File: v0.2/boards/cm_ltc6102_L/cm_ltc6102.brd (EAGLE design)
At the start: 81 x 60 mm, 98 parts, among them J1 10118194-0001LF, U1 ADA4528-2ARMZ-R7, U10 TS5A3159ADBVRDBV6-M, U2 LTC6102IMS8PBF, U3 ADM7170ACPZ-1.3-R7CP_8_21-M, U4 MIC2250-1YD5TSOT-23-5_D5-M, U6 TS3A4751PWRPW14-M, U7 TS5A4624DCKRDCK6-M, X1 PN87520-S

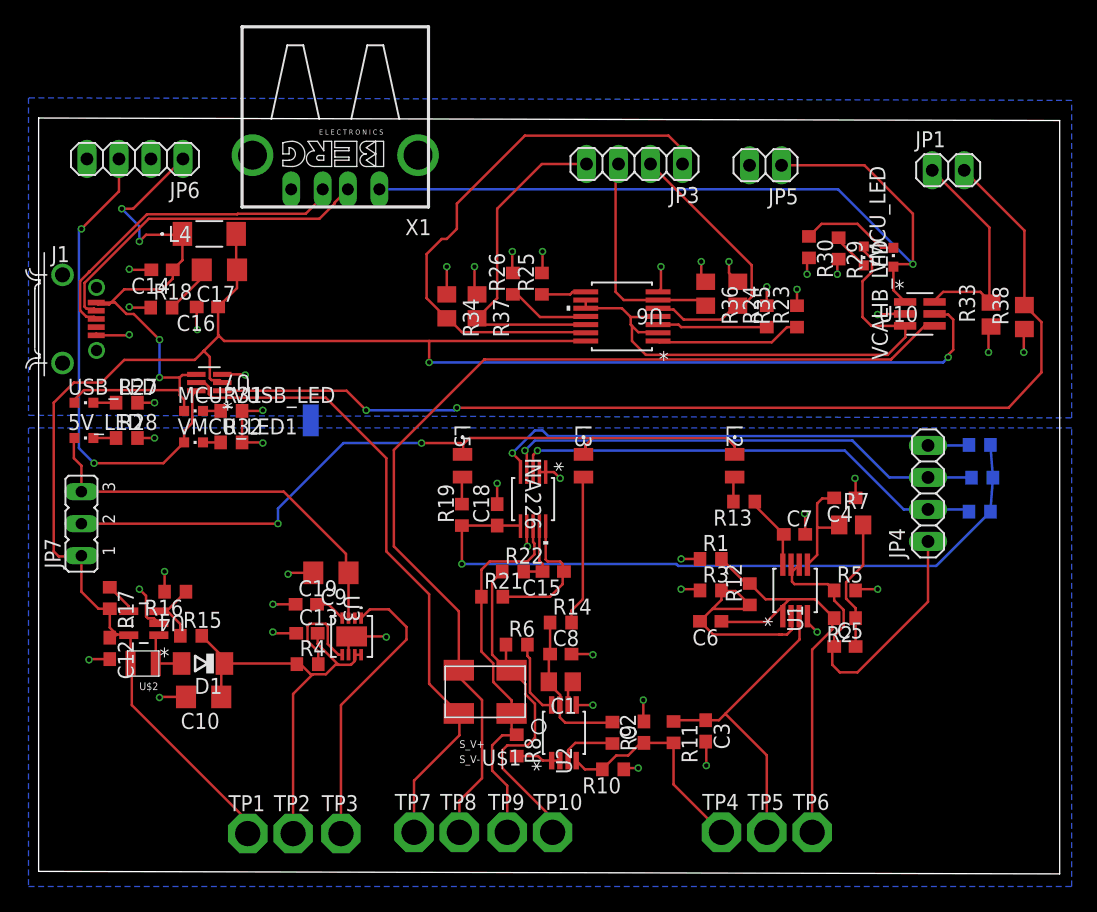
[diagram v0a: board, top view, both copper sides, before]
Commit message: cm_ltc6102_L: modify layout, finish silkscreen
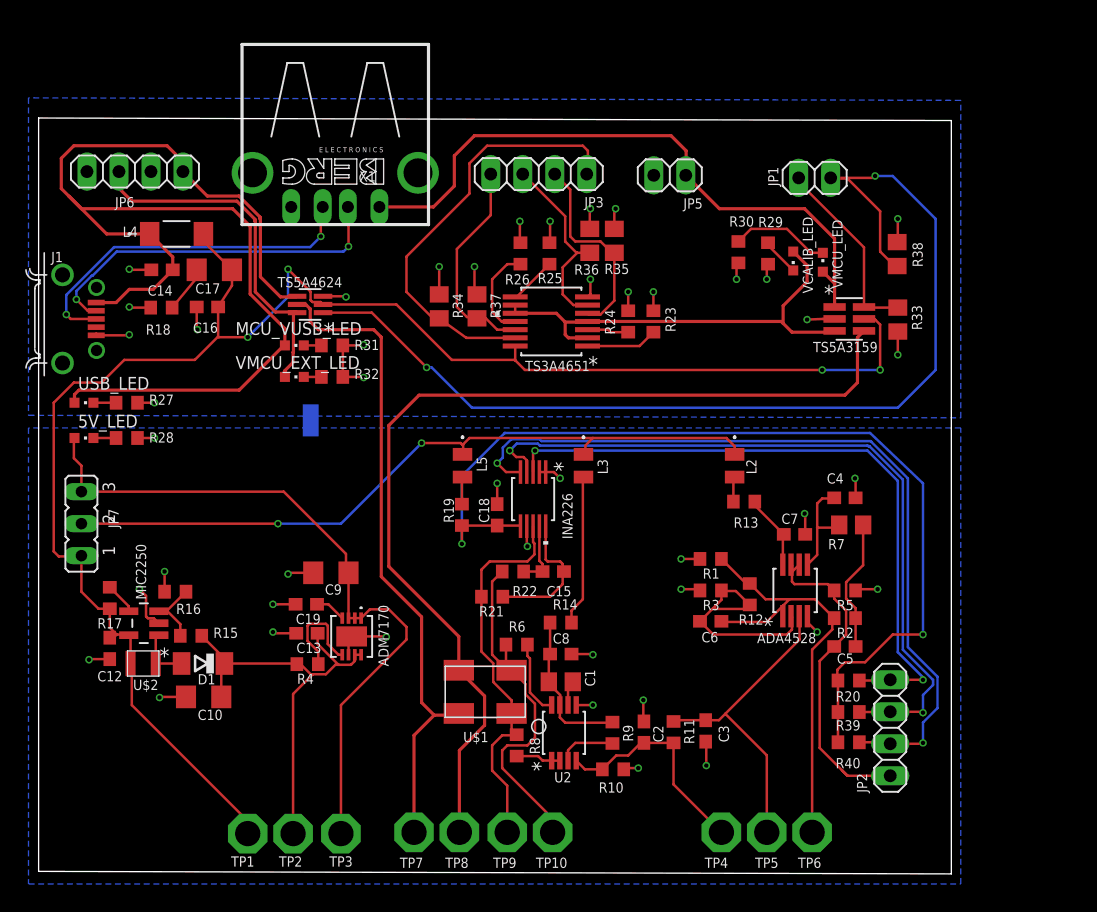
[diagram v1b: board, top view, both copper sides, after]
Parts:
- removed JP4: (no value), pinhead:1X04
- removed U10: TS5A3159ADBVRDBV6-M, texas_instruments:DBV6-M
- removed U6: TS3A4751PWRPW14-M, texas_instruments:PW14-M
- removed U7: TS5A4624DCKRDCK6-M, texas_instruments:DCK6-M
- removed VMCU_LED1: (no value), led:CHIPLED_0603
- added JP2: (no value), pinhead:1X04
- added TS3A4651: TS3A4751PWRPW14-M, texas_instruments:PW14-M
- added TS5A3159: TS5A3159ADBVRDBV6-M, texas_instruments:DBV6-M
- added TS5A4624: TS5A4624DCKRDCK6-M, texas_instruments:DCK6-M
- added VMCU_EXT_LED: (no value), led:CHIPLED_0603
- moved R40 25.8 mm to (64.3, 10.2), flipped to the top
- moved R39 21.4 mm to (64.3, 12.7), flipped to the top
- moved R20 17.0 mm to (64.3, 15.2), flipped to the top
- moved R23 11.4 mm to (48.8, 43.6)
- moved R38 11.3 mm to (68.2, 49.0), turned to 270 degrees
- moved R24 11.0 mm to (46.8, 43.6)
- moved R35 10.7 mm to (45.7, 50.0)
- moved JP1 10.6 mm to (61.6, 55.0)
- moved R36 10.1 mm to (43.8, 50.0)
- moved MCU_VUSB_LED 9.54 mm to (20.3, 41.8)
- moved R31 9.54 mm to (23.3, 41.8)
- moved R32 9.54 mm to (23.3, 39.2)
- moved JP5 7.64 mm to (50.1, 55.2)
- moved JP3 7.64 mm to (39.7, 55.4)
- moved R33 7.41 mm to (68.2, 43.8)
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- renumbered U1 to ADA4528, U3 to ADM7170, U4 to MIC2250
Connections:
- net 5V_F: now also TS3A4651.14, TS5A3159.5, TS5A4624.2; no longer U10.5, U6.14, U7.2
- net 5V_USB: now also TS5A4624.4; no longer U7.4
- net ADC_CM_LOW: now also JP2.1; no longer JP4.1
- net ALERT: now also JP2.4; no longer JP4.2
- net DGND: now also TS3A4651.7, TS5A3159.2, TS5A4624.3; no longer U10.2, U6.7, U7.3
- net N$26: now also VMCU_EXT_LED.C; no longer VMCU_LED1.C
- net N$30: now also TS3A4651.1; no longer U6.1
- net N$31: now also TS3A4651.3; no longer U6.3
- net N$32: now also TS3A4651.8; no longer U6.8
- net N$33: now also TS3A4651.11; no longer U6.11
- net SCL: now also JP2.2; no longer JP4.4
- net SDA: now also JP2.3; no longer JP4.3
- net SW_CTRL_0: now also TS5A3159.6; no longer U10.6
- net SW_CTRL_1: now also TS3A4651.13; no longer U6.13
- net SW_CTRL_2: now also TS3A4651.5; no longer U6.5
- net SW_CTRL_3: now also TS3A4651.6; no longer U6.6
- net SW_CTRL_4: now also TS3A4651.12; no longer U6.12
- net SW_CTRL_PWR: now also TS5A4624.1; no longer U7.1
- net VIN: now also TS5A4624.5; no longer U7.5
- net VMCU: now also TS5A3159.1; no longer U10.1
- net VOUT: now also TS5A3159.4; no longer U10.4
- net V_CALIB: now also TS3A4651.10, TS3A4651.2, TS3A4651.4, TS3A4651.9, TS5A3159.3; no longer U10.3, U6.10, U6.2, U6.4, U6.9
- net V_EXT: now also TS5A4624.6, VMCU_EXT_LED.A; no longer U7.6, VMCU_LED1.A
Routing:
- net 5V_USB: track 48.1 -> 94.0 mm, vias 4 -> 0
- net SCL: track 39.4 -> 64.9 mm, vias 1 -> 2
- net SDA: track 39.0 -> 60.2 mm, vias 1 -> 2
- net INA_VCC: track 56.8 -> 76.9 mm, vias 1 -> 2
- net ALERT: track 38.1 -> 53.3 mm, vias 1 -> 2
- net VMCU: track 65.7 -> 51.4 mm, vias 1 -> 0
- net 5V_F: track 148.4 -> 134.5 mm, vias 2 -> 4
- net V_EXT: track 38.4 -> 28.4 mm, vias 2 -> 0
- net SW_CTRL_1: track 44.3 -> 34.3 mm
- net SW_CTRL_4: track 26.8 -> 17.0 mm
- net V_CALIB: track 44.4 -> 36.5 mm
- net SW_CTRL_2: track 22.4 -> 15.9 mm
- net N$30: track 11.6 -> 5.69 mm
- net N$31: track 8.71 -> 3.31 mm
- net SW_CTRL_3: track 17.9 -> 15.2 mm
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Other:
- board size 81 x 60 mm -> 72.5 x 60 mm
- board text added: "5.5V"
- board text added: "5V"
- board text added: "5V_F"
- board text added: "5V_R"
- board text added: "ADC"
- board text added: "ALT"
- board text added: "Current Measurement Board"
- board text added: "GND"
- board text added: "PWR"
- board text added: "S1_OUT"
- board text added: "S1_OUT_F"
- board text added: "S2_OUT"
- board text added: "SCL"
- board text added: "SDA"
- board text added: "SHUNT+"
- board text added: "SHUNT-"
- board text added: "SW"
- board text added: "SW0"
- board text added: "SW1"
- board text added: "SW2"
- board text added: "SW3"
- board text added: "SW4"
- board text added: "V0.2 ltc6102"
- board text added: "VEXT"
- board text added: "VIN"
- board text added: "VMCU"
- board text added: "VOUT"
- board text removed: "S_V+"
- board text removed: "S_V-"

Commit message: cm_ltc6102_L: fix wrong sized ic and surface capacitor
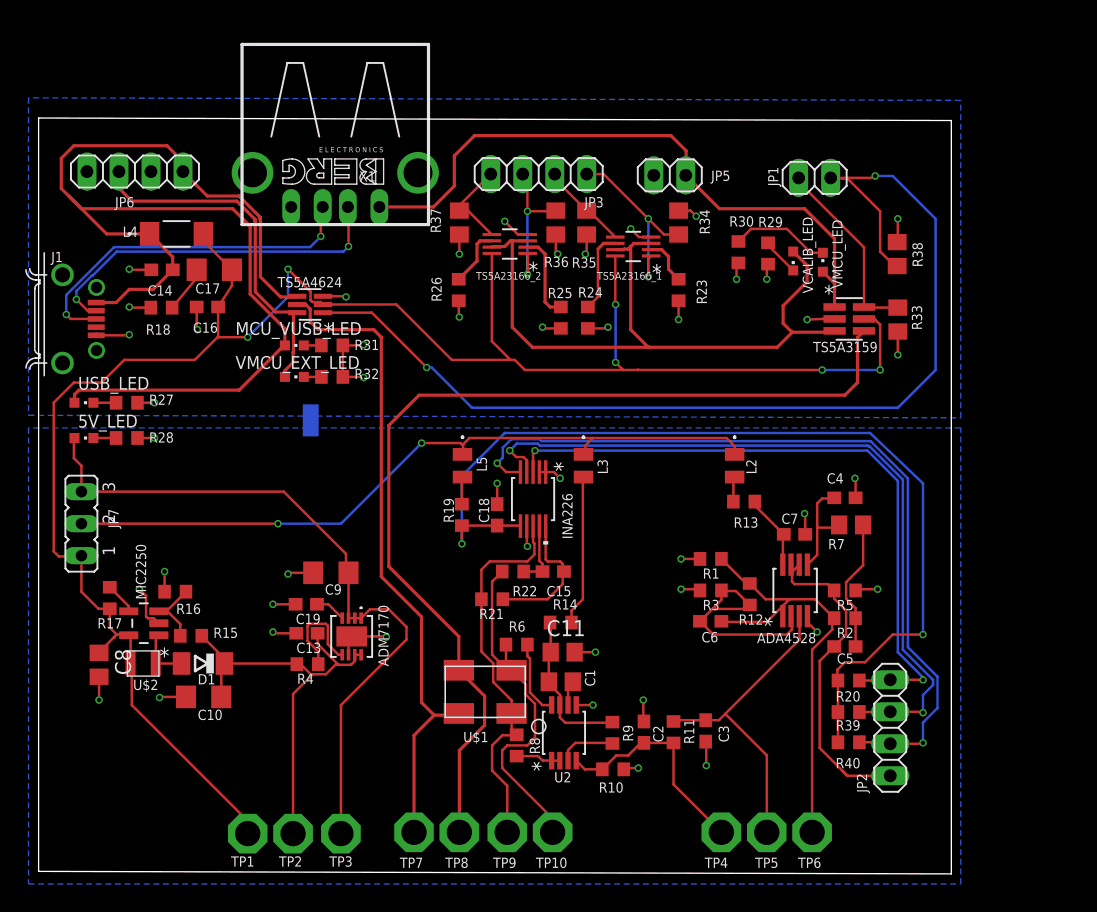
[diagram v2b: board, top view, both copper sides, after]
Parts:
- removed C12: 10uF x7R, rcl:C0603
- removed TS3A4651: TS3A4751PWRPW14-M, texas_instruments:PW14-M
- added C11: 10uF x7R, rcl:C0805
- added TS5A23166_1, TS5A23166_2: TS5A23166DCURDCU8-M, texas_instruments:DCU8-M
- C8: device rcl:C0603 -> rcl:C0805
- R12: value 100k 0.01% -> 100k 0.05%
- moved C8 36.7 mm to (4.80, 16.4), turned to 270 degrees
- moved R34 20.1 mm to (50.8, 51.5)
- moved R37 6.80 mm to (33.4, 51.5), turned to 90 degrees
- moved R26 5.69 mm to (33.4, 46.1), turned to 270 degrees
- moved R25 5.18 mm to (41.5, 44.0), turned to 270 degrees
- moved R24 3.21 mm to (43.6, 44.0), turned to 270 degrees
- moved R23 3.20 mm to (50.8, 46.1), turned to 270 degrees
- moved R36 3.06 mm to (41.0, 51.5), turned to 90 degrees
- moved R35 2.63 mm to (43.5, 51.5), turned to 90 degrees
- moved R21 0.20 mm to (36.0, 21.6)
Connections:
- net 5V_F: now also C8.1, TS5A23166_1.8, TS5A23166_2.8; no longer C12.1, TS3A4651.14
- net DGND: now also TS5A23166_1.4, TS5A23166_2.4; no longer TS3A4651.7
- net GND: now also C11.2; no longer C12.2
- net LTC_VCC: now also C11.1; no longer C8.1
- net N$30: now also TS5A23166_1.2; no longer TS3A4651.1
- net N$31: now also TS5A23166_1.6; no longer TS3A4651.3
- net N$32: now also TS5A23166_2.2; no longer TS3A4651.8
- net N$33: now also TS5A23166_2.6; no longer TS3A4651.11
- net SW_CTRL_1: now also TS5A23166_1.1; no longer TS3A4651.13
- net SW_CTRL_2: now also TS5A23166_1.5; no longer TS3A4651.5
- net SW_CTRL_3: now also TS5A23166_2.1; no longer TS3A4651.6
- net SW_CTRL_4: now also TS5A23166_2.5; no longer TS3A4651.12
- net V_CALIB: now also TS5A23166_1.3, TS5A23166_1.7, TS5A23166_2.3, TS5A23166_2.7; no longer TS3A4651.10, TS3A4651.2, TS3A4651.4, TS3A4651.9
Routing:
- net V_CALIB: track 36.5 -> 56.4 mm
- net 5V_F: track 134.5 -> 153.2 mm, vias 4 -> 6
- net SW_CTRL_1: track 34.3 -> 15.6 mm, vias 0 -> 2
- net SW_CTRL_4: track 17.0 -> 7.30 mm
- net SW_CTRL_2: track 15.9 -> 7.10 mm
- net N$33: track 7.91 -> 4.68 mm
- net N$31: track 3.31 -> 6.50 mm
- net SW_CTRL_3: track 15.2 -> 12.0 mm, vias 0 -> 2
- net N$32: track 3.80 -> 6.82 mm
- net N$30: track 5.69 -> 3.74 mm
- net DGND: track 41.6 -> 42.1 mm, vias 22 -> 23

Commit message: fix enable pull ups error, update bom
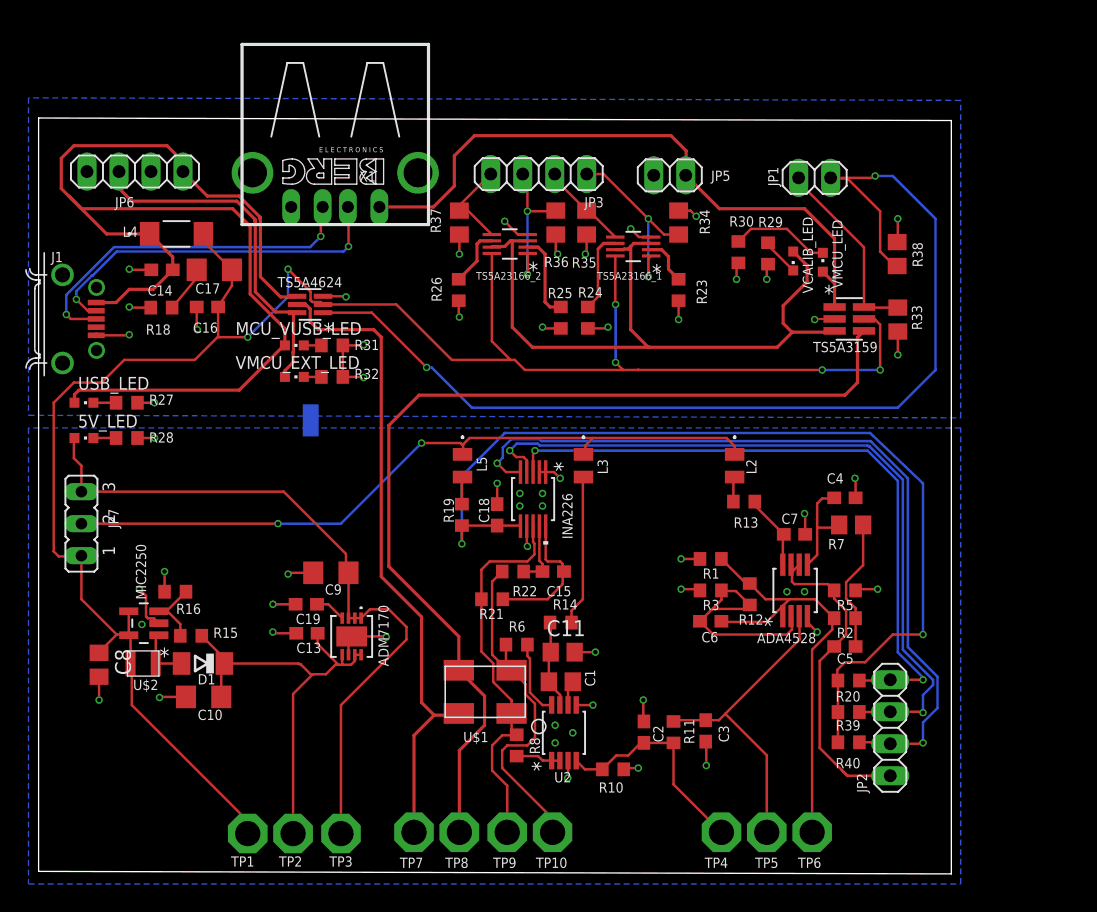
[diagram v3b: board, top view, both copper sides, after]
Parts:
- removed R17, R4, R9: 10k 1%, resistor:R0603
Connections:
- removed net N$15: ADM7170.5, R4.2
- removed net N$18: MIC2250.4, R17.1
- removed net N$5: R9.2, U2.3
- net 5.5V: now also ADM7170.5; no longer R4.1
- net 5V_F: now also MIC2250.4; no longer R17.2
- net GND: now also U2.3
- net LTC_VCC: no longer R9.1
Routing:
- net N$15: track 8.09 -> 0.00 mm
- net LTC_VCC: track 12.4 -> 7.01 mm
- net N$5: track 4.62 -> 0.00 mm
- net N$18: track 2.52 -> 0.00 mm
- net GND: track 43.6 -> 45.0 mm, vias 23 -> 24
- net 5V_F: track 153.2 -> 154.4 mm
- net 5.5V: track 34.5 -> 35.2 mm
- net DGND: track 42.1 -> 41.5 mm

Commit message: cm_ltc6102: increase track size add doc
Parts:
- C1: value 0.1uF X7R -> 100nF x7R; device rcl:C0805 -> rcl:C0603
- moved R10 2.90 mm to (45.5, 11.0), turned to 270 degrees
- moved L5 0.20 mm to (33.6, 32.0)
- moved C1 0.16 mm to (41.4, 15.2), turned to 0 degrees
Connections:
- net LTC_VCC: now also C1.1; no longer C1.2
- net N$6: now also C1.2; no longer C1.1
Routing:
- net 5.5V: track 35.2 -> 44.2 mm
- net GND: track 45.0 -> 37.5 mm, vias 24 -> 25
- net DGND: track 41.5 -> 34.4 mm
- net 5V_USB: track 94.0 -> 87.5 mm
- net ALERT: track 53.3 -> 49.6 mm, vias 2 -> 1
- net VMCU: track 51.4 -> 48.3 mm
- net SHUNT_V-: track 28.5 -> 25.7 mm
- net N$11: track 17.9 -> 15.2 mm
- net N$7: track 8.55 -> 6.75 mm
- net ADC_CM_LOW: track 27.0 -> 25.2 mm
- net SCL: track 64.9 -> 66.3 mm, vias 2 -> 1
- net D-: track 28.8 -> 27.5 mm
- net N$13: track 11.1 -> 9.97 mm
- net S1_OUT: track 17.6 -> 18.7 mm
- net INA_VCC: track 76.9 -> 77.9 mm
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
